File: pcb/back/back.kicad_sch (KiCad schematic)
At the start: 59 parts, among them J1 Conn_01x02, J2 USB_B_Micro, U1 ATSAMD21G18A-A, U2 LIS3DH, U3 XC6206PxxxMR, U4 TP4057

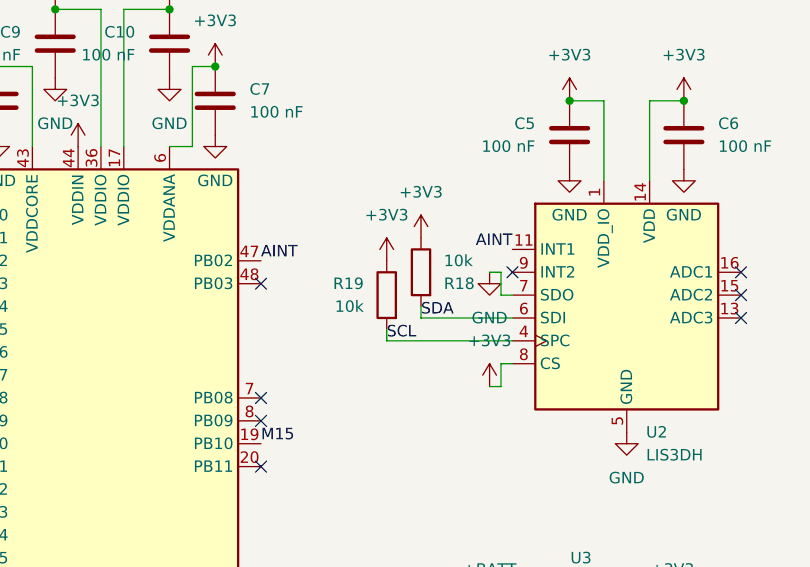
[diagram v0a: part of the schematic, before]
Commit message: Use 2k I2C resistors
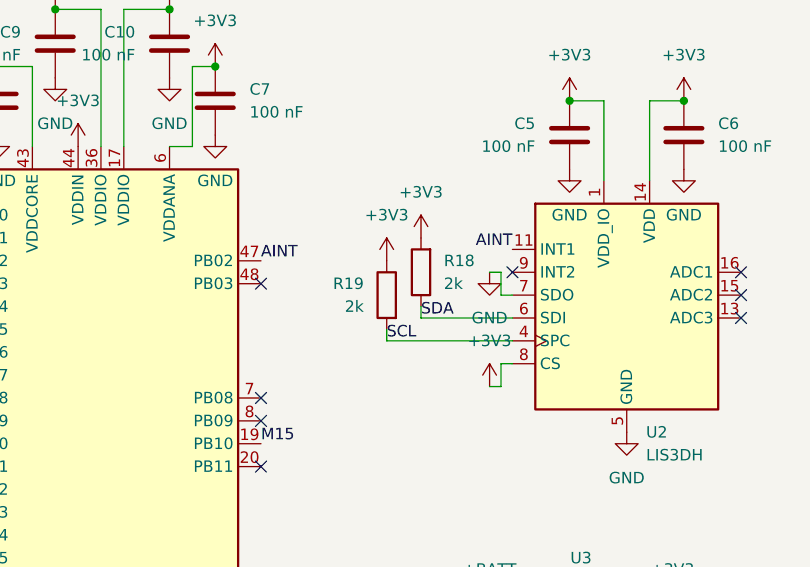
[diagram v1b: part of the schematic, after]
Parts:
- R18, R19: value 10k -> 2k
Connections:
- net +3V3: now also R18.2; no longer R18.1
- net SDA: now also R18.1; no longer R18.2
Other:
- moved on the sheet: R18
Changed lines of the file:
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@@
 			)
 		)
-		(property "Value" "10k"
+		(property "Value" "2k"
 			(at 176.53 64.7699 0)
 			(show_name no)
@@
 	(symbol
 		(lib_id "Device:R")
-		(at 182.88 60.96 0)
-		(mirror y)
+		(at 182.88 60.96 180)
 		(unit 1)
 		(body_style 1)
@@
 		(dnp no)
 		(property "Reference" "R18"
-			(at 185.42 62.2301 0)
+			(at 185.42 59.6899 0)
 			(show_name no)
 			(do_not_autoplace no)
@@
 			)
 		)
-		(property "Value" "10k"
-			(at 185.42 59.6901 0)
-			(show_name no)
-			(do_not_autoplace no)
+		(property "Value" "2k"
+			(at 185.42 62.2299 0)
+			(show_name no)
+			(do_not_autoplace no)

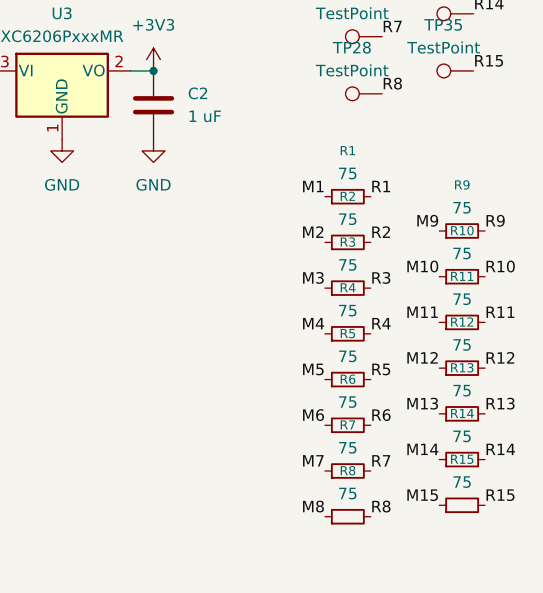
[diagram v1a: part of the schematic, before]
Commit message: Update LED resistors
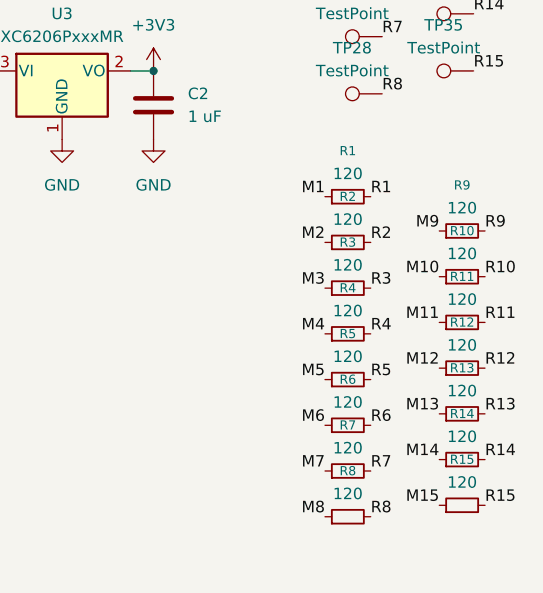
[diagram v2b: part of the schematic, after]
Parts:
- R1, R10, R11, R12, R13, R14, R15, R2, R3, R4, R5, R6, R7, R8, R9: value 75 -> 120
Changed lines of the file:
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@@
 			)
 		)
-		(property "Value" "75"
+		(property "Value" "120"
 			(at 232.41 140.97 90)
 			(show_name no)
@@
 			)
 		)
-		(property "Value" "75"
+		(property "Value" "120"
 			(at 245.11 119.38 90)
 			(show_name no)
@@
 			)
 		)
-		(property "Value" "75"
+		(property "Value" "120"
 			(at 245.11 124.46 90)
 			(show_name no)
@@
 			)
 		)
-		(property "Value" "75"
+		(property "Value" "120"
 			(at 232.41 146.05 90)
 			(show_name no)
@@
 			)
 		)
-		(property "Value" "75"
+		(property "Value" "120"
 			(at 232.41 120.65 90)
 			(show_name no)
@@
 			)
 		)
-		(property "Value" "75"
+		(property "Value" "120"
 			(at 245.11 114.3 90)
 			(show_name no)
@@
 			)
 		)
-		(property "Value" "75"
+		(property "Value" "120"
 			(at 232.41 135.89 90)
 			(show_name no)
@@
 			)
 		)
-		(property "Value" "75"
+		(property "Value" "120"
 			(at 232.41 125.73 90)
 			(show_name no)
@@
 			)
 		)
-		(property "Value" "75"
+		(property "Value" "120"
 			(at 245.11 134.62 90)
 			(show_name no)
@@
 			)
 		)
-		(property "Value" "75"
+		(property "Value" "120"
 			(at 232.41 130.81 90)
 			(show_name no)
@@
 			)
 		)
-		(property "Value" "75"
+		(property "Value" "120"
 			(at 232.41 115.57 90)
 			(show_name no)
@@
 			)
 		)
-		(property "Value" "75"
+		(property "Value" "120"
 			(at 245.11 144.78 90)
 			(show_name no)
@@
 			)
 		)
-		(property "Value" "75"
+		(property "Value" "120"
 			(at 245.11 139.7 90)
 			(show_name no)
@@
 			)
 		)
-		(property "Value" "75"
+		(property "Value" "120"
 			(at 245.11 129.54 90)
 			(show_name no)
@@
 			)
 		)
-		(property "Value" "75"
+		(property "Value" "120"
 			(at 232.41 110.49 90)
 			(show_name no)
